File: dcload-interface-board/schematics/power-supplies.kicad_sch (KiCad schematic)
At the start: 7 parts, among them U100 L78L33

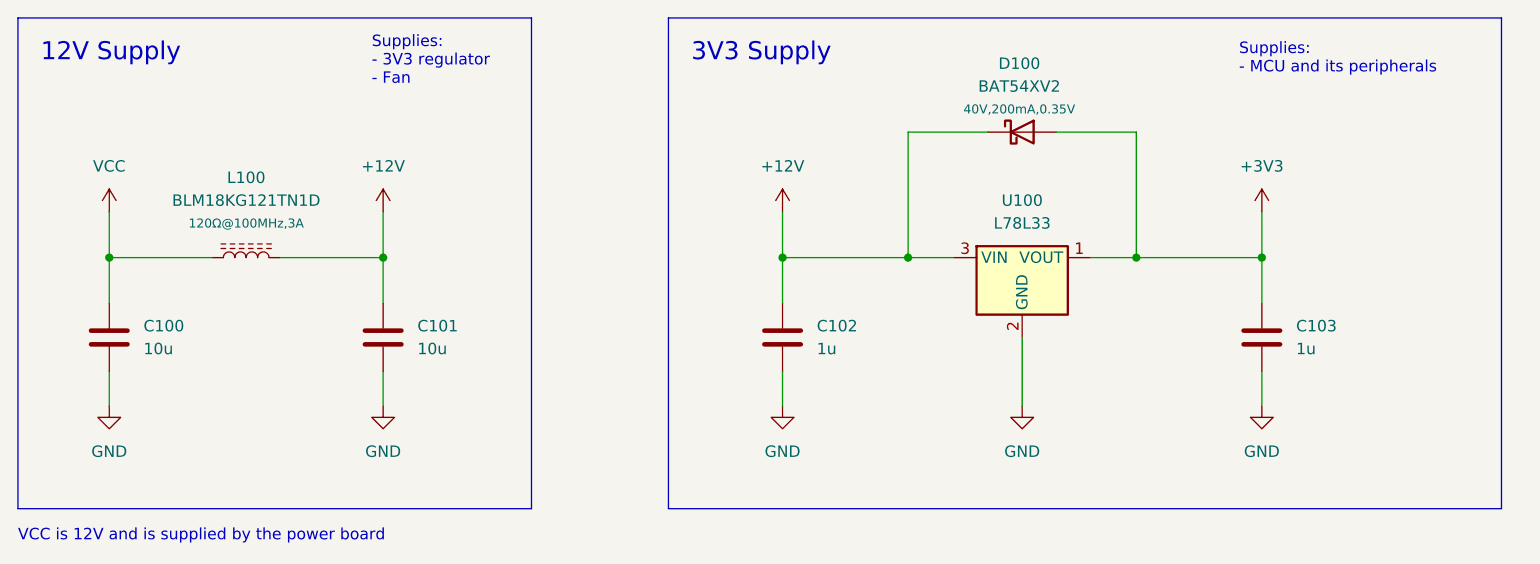
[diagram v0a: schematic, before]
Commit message: add: interface panel board
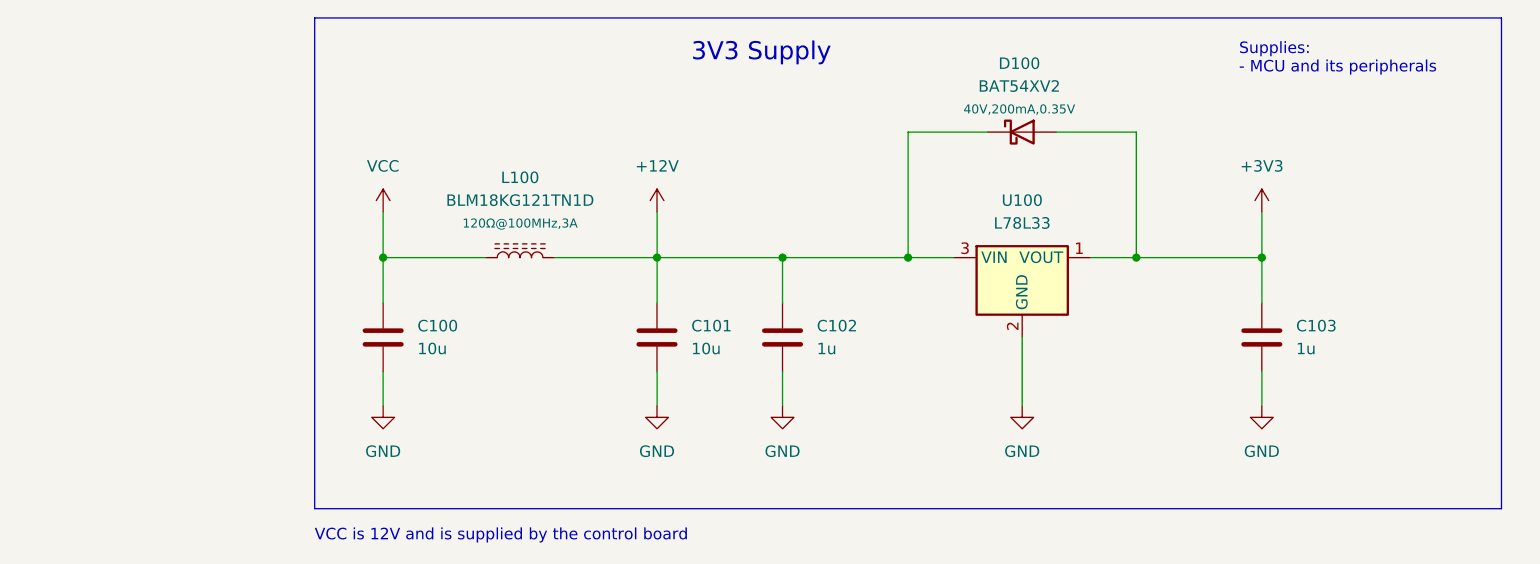
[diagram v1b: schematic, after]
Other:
- note added: "VCC is 12V and is supplied by the control board"
- note removed: "12V Supply"
- note removed: "Supplies: - 3V3 regulator - Fan"
- note removed: "VCC is 12V and is supplied by the power board"
- moved on the sheet: C100, C101, L100
